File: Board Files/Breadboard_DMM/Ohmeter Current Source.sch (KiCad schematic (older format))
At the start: 22 parts

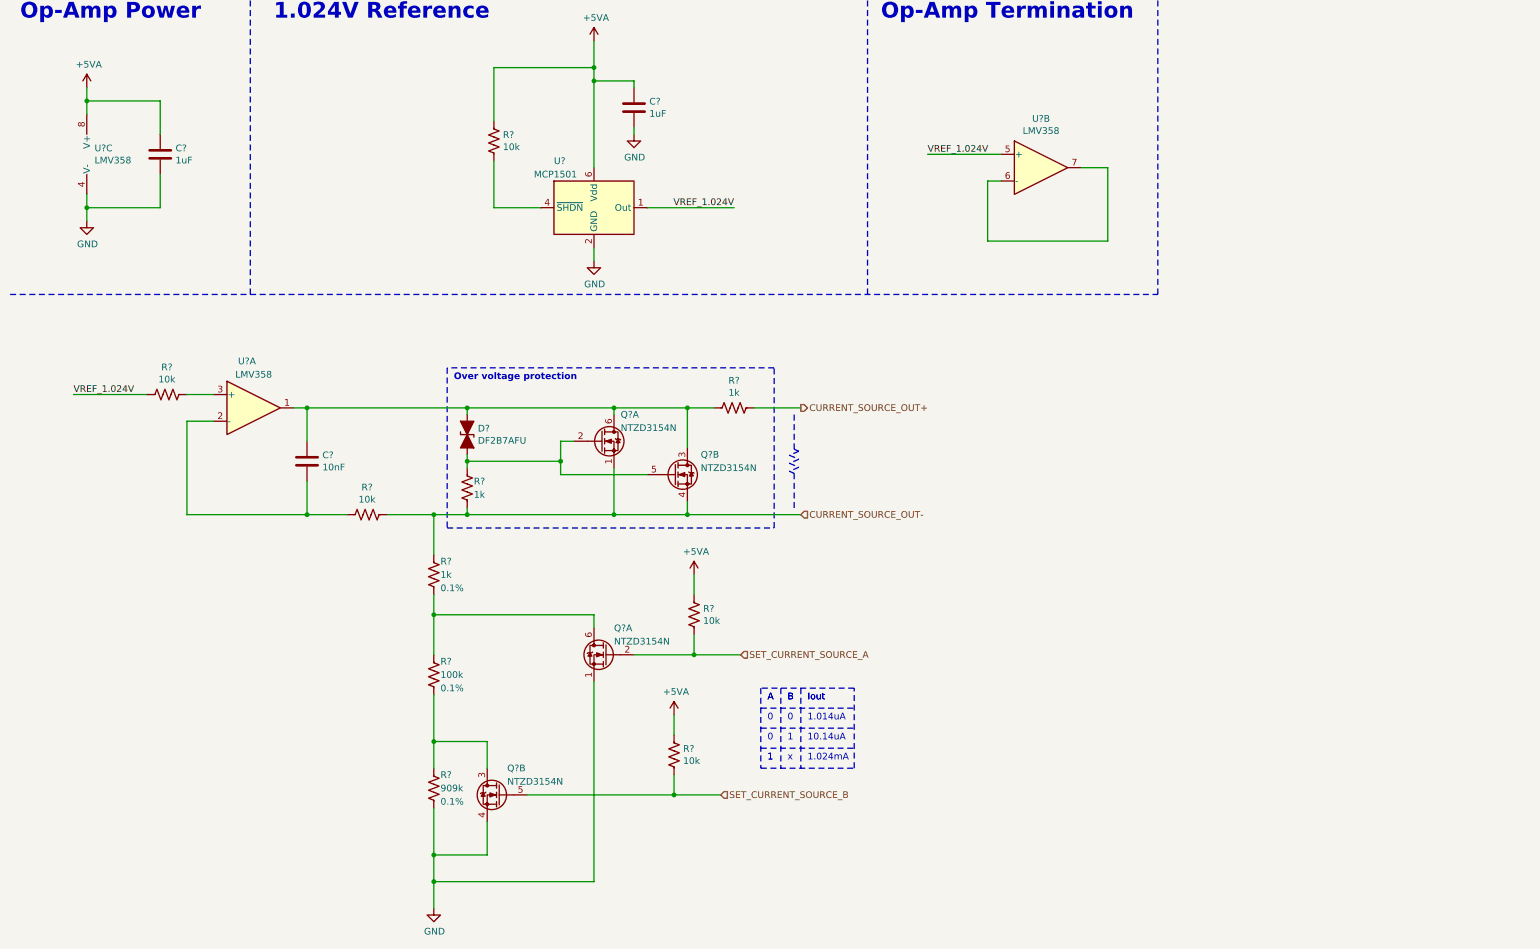
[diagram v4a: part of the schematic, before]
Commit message: Finished main cleanup, started adding digikey part numbers
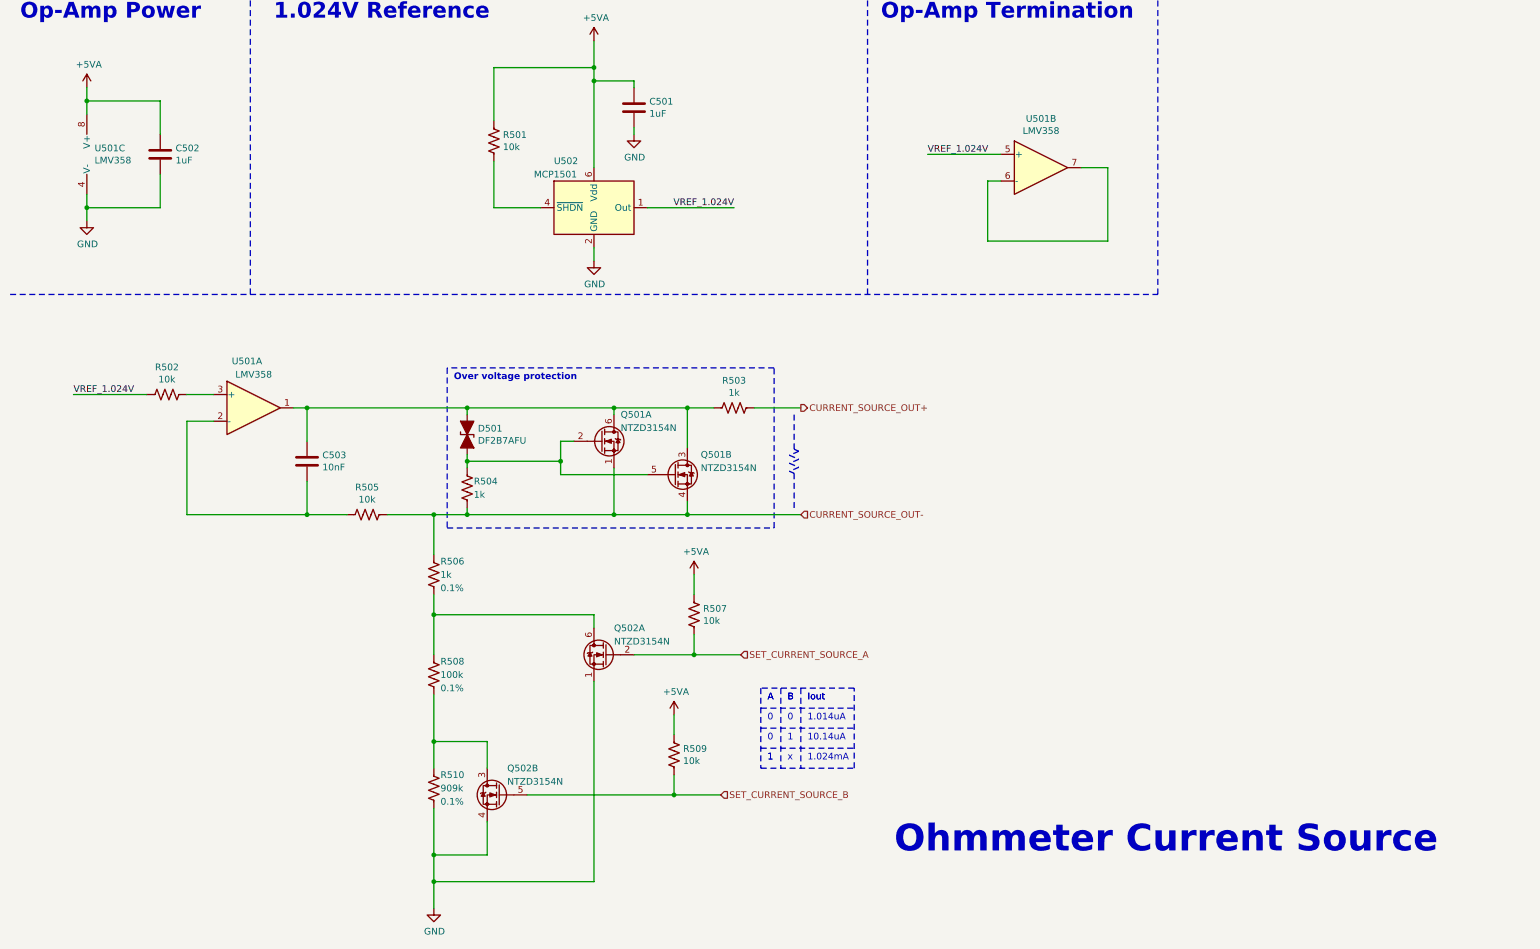
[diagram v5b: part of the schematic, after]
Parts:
- C501, C502, C503: renamed from C?; Digi-Key PN (none) -> -
- D501: renamed from D?; Digi-Key PN (none) -> -
- Q501, Q502: renamed from Q?; Digi-Key PN (none) -> -
- R501, R502, R503, R504, R505, R506, R507, R508, R509, R510: renamed from R?; Digi-Key PN (none) -> -
- U501, U502: renamed from U?; Digi-Key PN (none) -> -
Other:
- note added: "Ohmmeter Current Source"

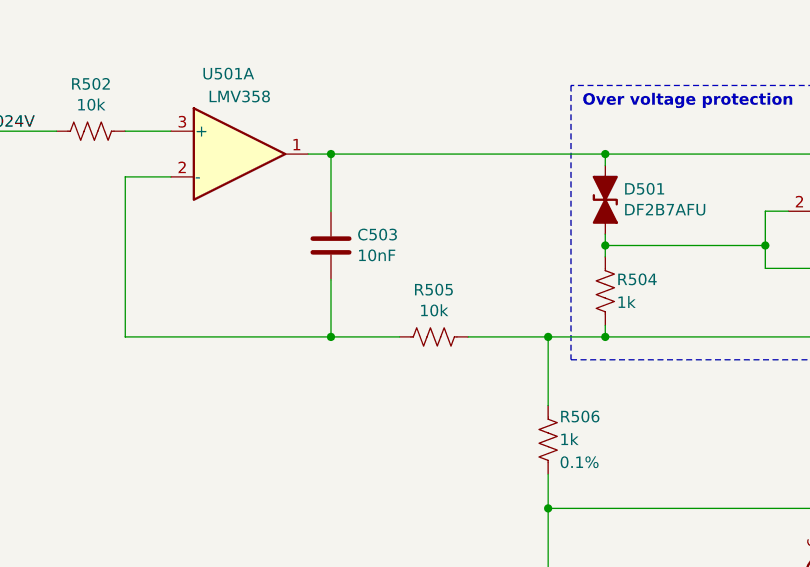
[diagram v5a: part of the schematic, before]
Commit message: Started adding Digikey links
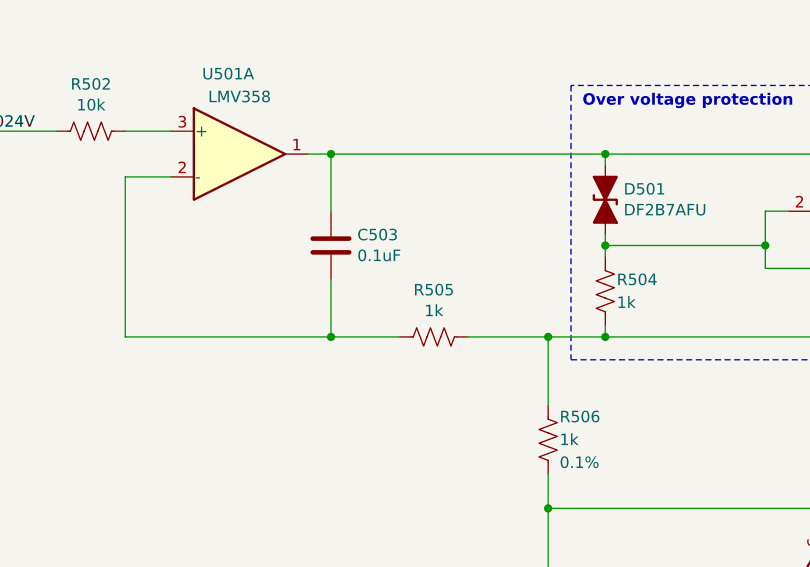
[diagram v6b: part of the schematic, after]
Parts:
- C503: value 10nF -> 0.1uF
- Q501, Q502: Digi-Key Link (none) -> https://www.digikey.com/en/products/detail/on-semiconductor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; Digi-Key PN - -> NTZD3154NT1GOSCT-ND
- R505: value 10k -> 1k
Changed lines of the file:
@@
 $Descr A4 11693 8268
 encoding utf-8
-Sheet 5 10
+Sheet 5 11
 Title "Toast-O-Meter"
-Date ""
+Date "2020-08-14"
 Rev "0"
 Comp ""
@@
 F 2 "Package_TO_SOT_SMD:SOT-563" H 4150 6450 50  0001 L CNN
 F 3 "https://www.onsemi.cn/PowerSolutions/document/NTZD3154N-D.PDF" H 4050 6550 50  0001 L CNN
-F 4 "" H 4050 6550 50  0001 C CNN "Digi-Key Link"
-F 5 "-" H 4050 6550 50  0001 C CNN "Digi-Key PN"
+F 4 "https://www.digikey.com/en/products/detail/on-semiconductor/NTZD3154NT1G/687137" H 4050 6550 50  0001 C CNN "Digi-Key Link"
+F 5 "NTZD3154NT1GOSCT-ND" H 4050 6550 50  0001 C CNN "Digi-Key PN"
 	2    4050 6550
 	-1   0    0    -1
@@
 F 2 "Package_TO_SOT_SMD:SOT-563" H 4950 5400 50  0001 L CNN
 F 3 "https://www.onsemi.cn/PowerSolutions/document/NTZD3154N-D.PDF" H 4850 5500 50  0001 L CNN
-F 4 "" H 4850 5500 50  0001 C CNN "Digi-Key Link"
-F 5 "-" H 4850 5500 50  0001 C CNN "Digi-Key PN"
+F 4 "https://www.digikey.com/en/products/detail/on-semiconductor/NTZD3154NT1G/687137" H 4850 5500 50  0001 C CNN "Digi-Key Link"
+F 5 "NTZD3154NT1GOSCT-ND" H 4850 5500 50  0001 C CNN "Digi-Key PN"
 	1    4850 5500
 	-1   0    0    -1
@@
 AR Path="/5F511849/5F7E68F4/5F51AFAC" Ref="R505"  Part="1"
 F 0 "R505" V 2945 4450 50  0000 C CNN
-F 1 "10k" V 3036 4450 50  0000 C CNN
+F 1 "1k" V 3036 4450 50  0000 C CNN
 F 2 "" V 3190 4440 50  0001 C CNN
 F 3 "~" H 3150 4450 50  0001 C CNN
@@
 AR Path="/5F511849/5F7E68F4/5F51AFA6" Ref="C503"  Part="1"
 F 0 "C503" H 2815 4096 50  0000 L CNN
-F 1 "10nF" H 2815 4005 50  0000 L CNN
+F 1 "0.1uF" H 2815 4005 50  0000 L CNN
 F 2 "" H 2738 3900 50  0001 C CNN
 F 3 "~" H 2700 4050 50  0001 C CNN
@@
 F 2 "Package_TO_SOT_SMD:SOT-563" H 5650 4050 50  0001 L CNN
 F 3 "https://www.onsemi.cn/PowerSolutions/document/NTZD3154N-D.PDF" H 5550 4150 50  0001 L CNN
-F 4 "" H 5550 4150 50  0001 C CNN "Digi-Key Link"
-F 5 "-" H 5550 4150 50  0001 C CNN "Digi-Key PN"
+F 4 "https://www.digikey.com/en/products/detail/on-semiconductor/NTZD3154NT1G/687137" H 5550 4150 50  0001 C CNN "Digi-Key Link"
+F 5 "NTZD3154NT1GOSCT-ND" H 5550 4150 50  0001 C CNN "Digi-Key PN"
 	2    5550 4150
 	1    0    0    -1
@@
 F 2 "Package_TO_SOT_SMD:SOT-563" H 5100 3800 50  0001 L CNN
 F 3 "https://www.onsemi.cn/PowerSolutions/document/NTZD3154N-D.PDF" H 5000 3900 50  0001 L CNN
-F 4 "" H 5000 3900 50  0001 C CNN "Digi-Key Link"
-F 5 "-" H 5000 3900 50  0001 C CNN "Digi-Key PN"
+F 4 "https://www.digikey.com/en/products/detail/on-semiconductor/NTZD3154NT1G/687137" H 5000 3900 50  0001 C CNN "Digi-Key Link"
+F 5 "NTZD3154NT1GOSCT-ND" H 5000 3900 50  0001 C CNN "Digi-Key PN"
 	1    5000 3900
 	1    0    0    -1

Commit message: Finished adding parts, cleaned up, ran ERC
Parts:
- added R508, R512: 100, Resistor_SMD:R_0603_1608Metric_Pad1.05x0.95mm_HandSolder, symbol Device:R_US
- C501, C502: footprint (none) -> Resistor_SMD:R_0603_1608Metric_Pad1.05x0.95mm_HandSolder; Digi-Key Link (none) -> https://www.digikey.com/en/products/detail/samsung-electro-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; Digi-Key PN - -> 1276-6524-1-ND
- C503: footprint (none) -> Resistor_SMD:R_0603_1608Metric_Pad1.05x0.95mm_HandSolder; Digi-Key Link (none) -> https://www.digikey.com/en/products/detail/samsung-electro-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; Digi-Key PN - -> 1276-1006-1-ND
- D501: Digi-Key Link (none) -> https://www.digikey.com/en/products/detail/toshiba-semicond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; Digi-Key PN - -> DF2B7AFUH3FCT-ND
- R501, R502, R507: footprint (none) -> Resistor_SMD:R_0603_1608Metric_Pad1.05x0.95mm_HandSolder; Digi-Key Link (none) -> https://www.digikey.com/en/products/detail/yageo/RC0603FR-0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; Digi-Key PN - -> 311-10.0KHRCT-ND
- R503, R504, R505: footprint (none) -> Resistor_SMD:R_0603_1608Metric_Pad1.05x0.95mm_HandSolder; Digi-Key Link (none) -> https://www.digikey.com/en/products/detail/yageo/RC0603FR-0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; Digi-Key PN - -> 311-1.00KHRCT-ND
- R506: footprint (none) -> Resistor_SMD:R_0805_2012Metric_Pad1.15x1.40mm_HandSolder; Digi-Key Link (none) -> https://www.digikey.com/en/products/detail/yageo/RT0805BRD0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; Digi-Key PN - -> YAG1820CT-ND
- R509: renamed from R508; footprint (none) -> Resistor_SMD:R_0805_2012Metric_Pad1.15x1.40mm_HandSolder; Digi-Key Link (none) -> https://www.digikey.com/en/products/detail/yageo/RT0805BRD0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; Digi-Key PN - -> YAG1759CT-ND
- R510: renamed from R509; footprint (none) -> Resistor_SMD:R_0603_1608Metric_Pad1.05x0.95mm_HandSolder; Digi-Key Link (none) -> https://www.digikey.com/en/products/detail/yageo/RC0603FR-0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; Digi-Key PN - -> 311-10.0KHRCT-ND
- R511: renamed from R510; value 909k -> 910k; footprint (none) -> Resistor_SMD:R_0805_2012Metric_Pad1.15x1.40mm_HandSolder; Digi-Key Link (none) -> https://www.digikey.com/en/products/detail/yageo/RT0805BRD0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; Digi-Key PN - -> YAG1993CT-ND
- U501: footprint (none) -> Package_SO:SOIC-8_3.9x4.9mm_P1.27mm; Digi-Key Link (none) -> https://www.digikey.com/en/products/detail/texas-instrument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; Digi-Key PN - -> 296-47593-1-ND
- U502: Digi-Key Link (none) -> https://www.digikey.com/en/products/detail/microchip-techno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; Digi-Key PN - -> MCP1501T-10E/CHYCT-ND
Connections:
- net SET_CURRENT_SOURCE_A: now also R508.2; no longer Q502.2 (G1), R507.2
- net SET_CURRENT_SOURCE_B: now also R512.2; no longer Q502.5 (G2), R510.2
- new net: Q502.2 (G1), R507.2, R508.1
- new net: Q502.5 (G2), R510.2, R512.1
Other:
- note added: "1.013uA"
- note removed: "1.014uA"
- moved on the sheet: C501, C503, D501, Q501A, Q501B, Q502A, Q502B, R501, R502, R503, R504, R505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

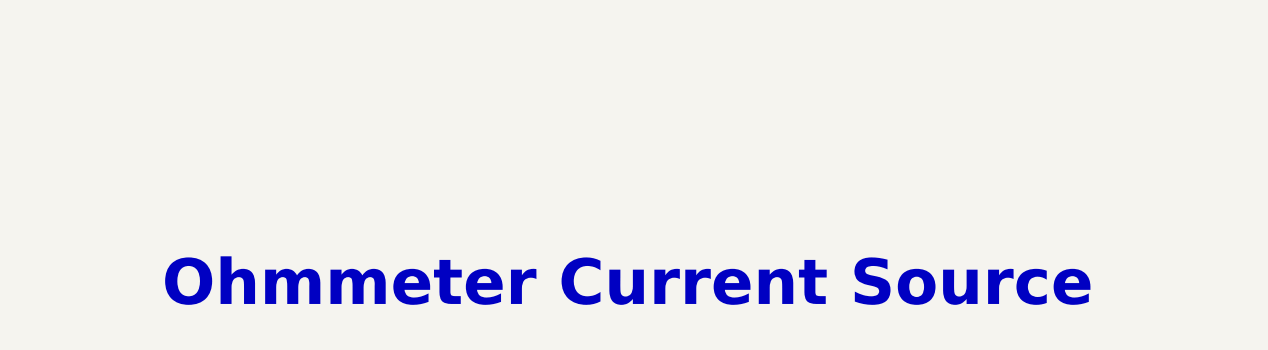
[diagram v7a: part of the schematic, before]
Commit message: Updated probe connector arrangement
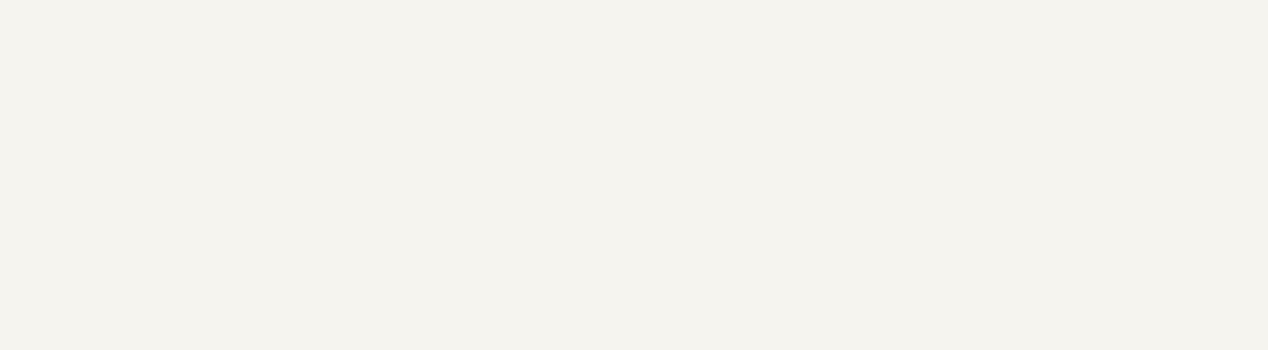
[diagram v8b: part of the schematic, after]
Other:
- note removed: "Ohmmeter Current Source"
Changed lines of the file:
@@
 Sheet 4 8
 Title "Toast-O-Meter"
-Date "2020-08-14"
+Date "2020-10-06"
 Rev "0"
 Comp ""
-Comment1 ""
+Comment1 "Isaac Rex"
 Comment2 ""
 Comment3 ""
@@
 	-1   0    0    1
 $EndComp
-Text Notes 12400 9750 0    200  ~ 40
-Ohmmeter Current Source
-$Comp
-L Device:R_US R?
+$Comp
+L Device:R_US R?
